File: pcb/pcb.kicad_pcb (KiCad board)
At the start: 2 copper layers, 65.5 x 70.5 mm, 22 parts, among them J1 Pump Back, J10 Temp & RH I2C, J2 Pump Front, J3 Electrovalve, J4 GPS, J5 Power, J6 APM, J7 Flowmeter, J8 OPC, J9 Pressure I2C, U1 LoRa, U2 MICRO SD

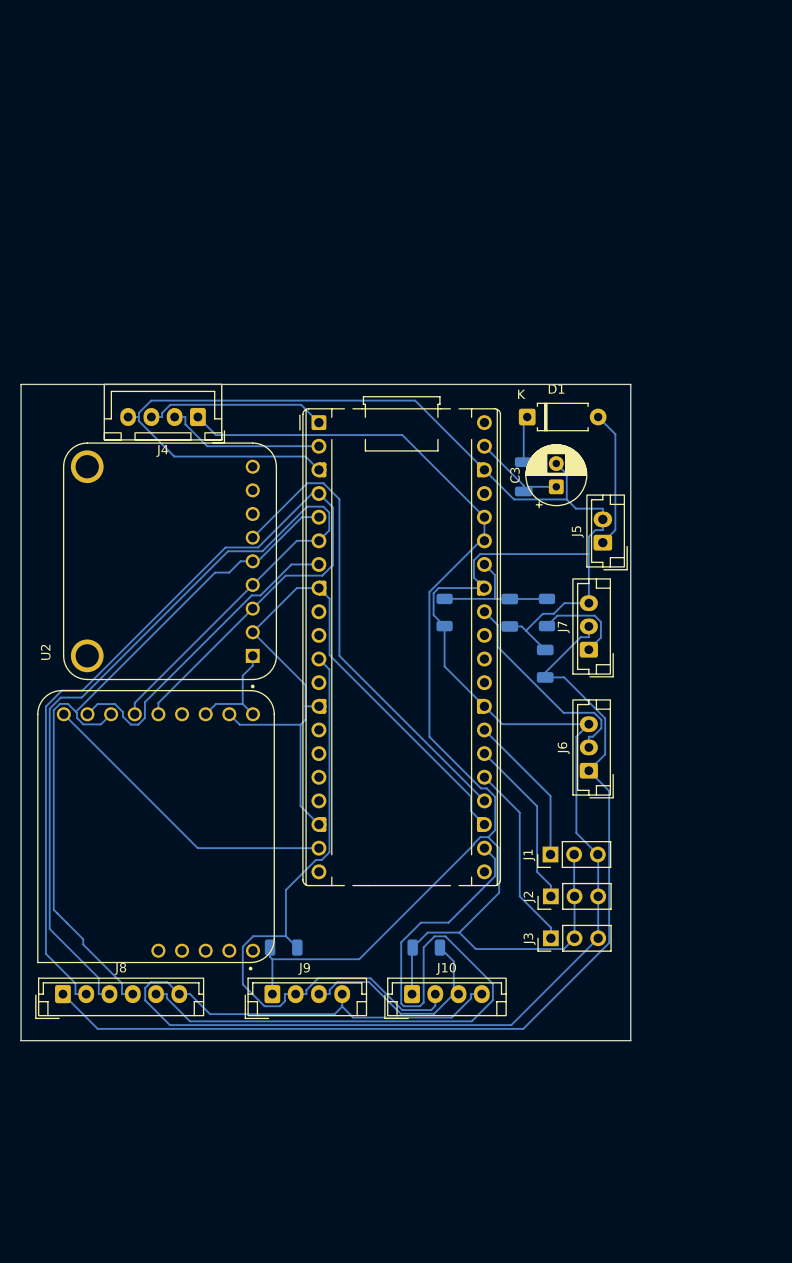
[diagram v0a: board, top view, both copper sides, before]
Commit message: New components layout
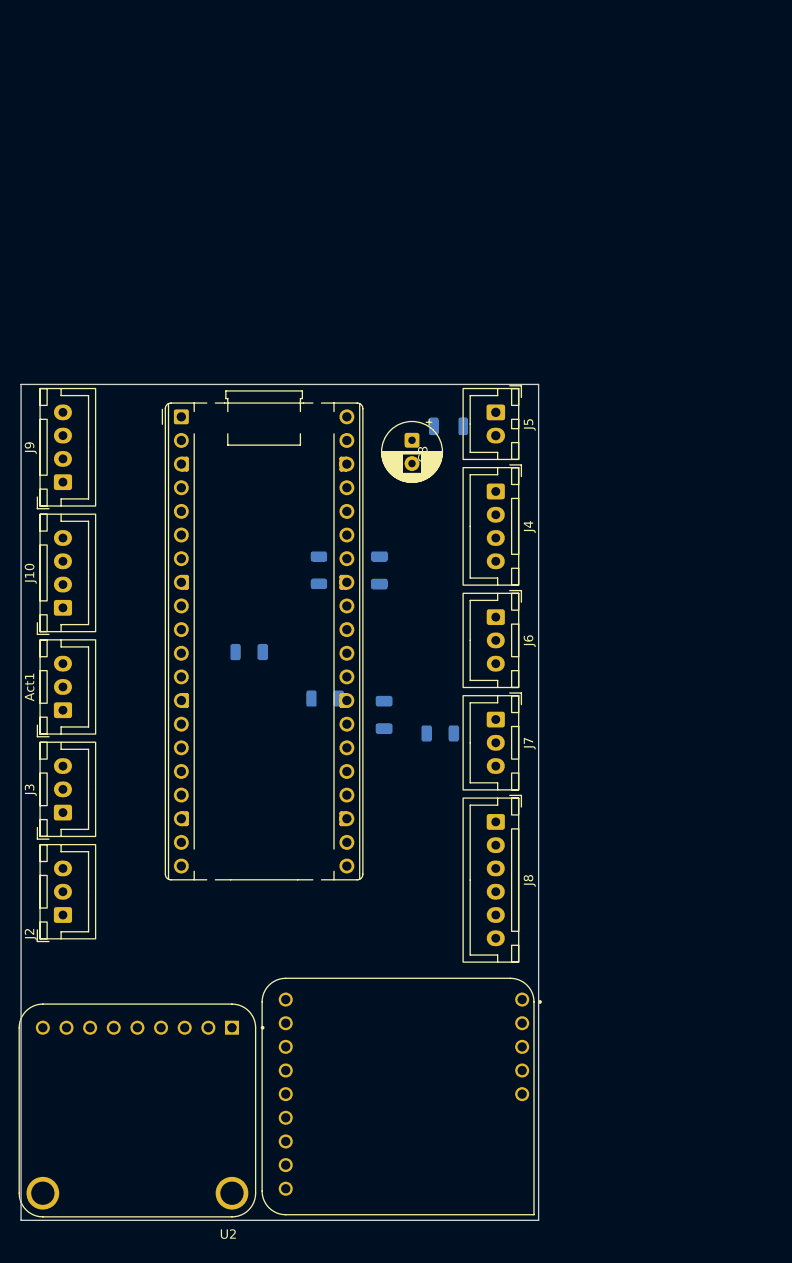
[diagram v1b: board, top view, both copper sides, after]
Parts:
- removed D1: D_Schottky, Diode_THT:D_A-405_P7.62mm_Horizontal
- Act1: renamed from J1; footprint Connector_PinHeader_2.54mm:PinHeader_1x03_P2.54mm_Vertical -> Connector_JST:JST_XH_B3B-XH-A_1x03_P2.50mm_Vertical
- J10, J9: footprint Connector_JST:JST_EH_B4B-EH-A_1x04_P2.50mm_Vertical -> Connector_JST:JST_XH_B4B-XH-A_1x04_P2.50mm_Vertical
- J2, J3: footprint Connector_PinHeader_2.54mm:PinHeader_1x03_P2.54mm_Vertical -> Connector_JST:JST_XH_B3B-XH-A_1x03_P2.50mm_Vertical
- J5: footprint Connector_JST:JST_EH_B2B-EH-A_1x02_P2.50mm_Vertical -> Connector_JST:JST_XH_B2B-XH-A_1x02_P2.50mm_Vertical
- J6, J7: footprint Connector_JST:JST_EH_B3B-EH-A_1x03_P2.50mm_Vertical -> Connector_JST:JST_XH_B3B-XH-A_1x03_P2.50mm_Vertical
- J8: footprint Connector_JST:JST_EH_B6B-EH-A_1x06_P2.50mm_Vertical -> Connector_JST:JST_XH_B6B-XH-A_1x06_P2.50mm_Vertical
- moved J9 59.4 mm to (105.0, 52.5), turned to 90 degrees
- moved U2 59.1 mm to (113.0, 120.0), turned to 180 degrees
- moved J10 55.9 mm to (105.0, 66.0), turned to 90 degrees
- moved Act1 54.6 mm to (105.0, 77.0)
- moved J3 54.1 mm to (105.0, 88.0)
- moved J2 52.5 mm to (105.0, 99.0)
- moved J8 50.0 mm to (151.5, 89.0), turned to -90 degrees
- moved U1 38.9 mm to (141.0, 118.5), turned to 0 degrees
- moved J4 33.0 mm to (151.5, 53.5), turned to -90 degrees
- moved R1 32.0 mm to (125.0, 70.8), turned to 180 degrees
- moved R2 28.9 mm to (133.2, 75.8), turned to 180 degrees
- moved J6 19.3 mm to (151.5, 67.0), turned to -90 degrees
- moved C2 18.2 mm to (139.5, 77.5)
- moved J5 18.1 mm to (151.5, 45.0), turned to -90 degrees
- moved R3 17.3 mm to (145.5, 79.5), turned to 180 degrees
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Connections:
- A1 pad 39: /3.3Vin -> /VSYS
- C3 pad 1: /3.3Vin -> /VSYS
- FB1 pad 1: Net-(D1-K) -> Net-(J5-Pin_1)
- FB1 pad 2: /3.3Vin -> /VSYS
- J5 pad 1: Net-(D1-A) -> Net-(J5-Pin_1)
- U1 pad JP3_1: /3.3V -> /VSYS
- U2 pad 1: /3.3V -> /VSYS
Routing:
- net GND: track 351.6 -> 0.00 mm
- net /3.3V: track 167.1 -> 0.00 mm
- net /SPI_SCK: track 106.6 -> 0.00 mm
- net /5V: track 106.0 -> 0.00 mm
- net /SPI_MISO: track 105.0 -> 0.00 mm
- net /OPC_CS: track 82.1 -> 0.00 mm
- net /SPI_MOSI: track 77.6 -> 0.00 mm
- net /I2C_SDA: track 69.9 -> 0.00 mm
- net /SD_CS: track 51.3 -> 0.00 mm
- net /LORA_CS: track 34.6 -> 0.00 mm
- net /LORA_RST: track 33.4 -> 0.00 mm
- net /I2C_SCL: track 23.7 -> 0.00 mm
- net /BAT_VOLT_ADC: track 22.5 -> 0.00 mm
- net /VALVE: track 20.3 -> 0.00 mm
- net /GPS_TX: track 19.6 -> 0.00 mm
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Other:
- board size 65.5 x 70.5 mm -> 55.6 x 89.8 mm

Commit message: new layout
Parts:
- moved Act1 49.9 mm to (151.5, 95.0), turned to -90 degrees
- moved J4 46.5 mm to (105.0, 52.5), turned to 90 degrees
- moved J9 27.0 mm to (105.0, 79.5)
- moved J7 24.0 mm to (151.5, 54.0)
- moved R2 19.7 mm to (113.5, 74.0), turned to 0 degrees
- moved R3 17.8 mm to (142.5, 62.0), turned to 90 degrees
- moved J3 13.5 mm to (105.0, 101.5)
- moved J8 12.5 mm to (151.5, 76.5)
- moved R1 11.6 mm to (113.5, 69.5), turned to 0 degrees
- moved J2 8.50 mm to (105.0, 90.5)
- moved U2 3.41 mm to (113.3, 116.6)
- moved C2 1.58 mm to (140.0, 76.0), turned to 180 degrees
- moved A1 1.52 mm to (118.5, 44.2)
- moved FB1 1.50 mm to (146.5, 45.0)
- moved J6 1.50 mm to (151.5, 65.5)
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
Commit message: v1 sent to JLCPCB
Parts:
- added SW1: SW_Push, Button_Switch_THT:SW_PUSH_6mm, F.Cu at (145.5, 71.5)
- moved R2 22.6 mm to (123.0, 53.5), turned to 180 degrees
- moved C2 18.6 mm to (146.5, 58.5), turned to -90 degrees
- moved J1 17.5 mm to (151.5, 77.5)
- moved R1 16.5 mm to (123.0, 56.0), turned to 180 degrees
- moved J8 12.5 mm to (151.5, 89.0)
- moved U2 2.89 mm to (113.5, 119.5)
- moved J3 2.50 mm to (105.0, 104.0)
- moved J2 2.00 mm to (105.0, 92.5)
- moved A1 1.76 mm to (118.5, 45.9)
- moved C3 1.50 mm to (142.5, 48.5)
- moved J9 1.50 mm to (105.0, 81.0)
- moved R3 1.08 mm to (143.0, 61.0), turned to 180 degrees
- moved J10 1.00 mm to (105.0, 67.0)
- moved C1 0.76 mm to (139.5, 62.5)
- moved FB1 0.50 mm to (146.5, 45.5)
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- renumbered Act1 to J1
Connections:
- A1 pad 10: unconnected-(A1-GPIO7-Pad10) -> /VALVE
- A1 pad 11: /I2C_SDA -> unconnected-(A1-GPIO8-Pad11)
- A1 pad 12: /I2C_SCL -> /SD_CS
- A1 pad 14: unconnected-(A1-GPIO10-Pad14) -> /SPI_SCK
- A1 pad 15: unconnected-(A1-GPIO11-Pad15) -> /SPI_MOSI
- A1 pad 16: unconnected-(A1-GPIO12-Pad16) -> /SPI_MISO
- A1 pad 19: /LORA_RST -> unconnected-(A1-GPIO14-Pad19)
- A1 pad 21: unconnected-(A1-GPIO16-Pad21) -> /LORA_CS
- A1 pad 24: /SD_CS -> unconnected-(A1-GPIO18-Pad24)
- A1 pad 25: /VALVE -> unconnected-(A1-GPIO19-Pad25)
- A1 pad 26: /PUMP_FRONT -> unconnected-(A1-GPIO20-Pad26)
- A1 pad 30: unconnected-(A1-RUN-Pad30) -> Net-(A1-RUN)
- A1 pad 4: /SPI_SCK -> /I2C_SDA
- A1 pad 5: /SPI_MOSI -> /I2C_SCL
- A1 pad 6: /SPI_MISO -> unconnected-(A1-GPIO4-Pad6)
- A1 pad 7: /LORA_CS -> unconnected-(A1-GPIO5-Pad7)
- A1 pad 9: unconnected-(A1-GPIO6-Pad9) -> /PUMP_FRONT
- J10 pad 2: /I2C_SDA -> /I2C_SCL
- J10 pad 3: /I2C_SCL -> /I2C_SDA
- J2 pad 1: /PUMP_FRONT -> GND
- J2 pad 3: GND -> /PUMP_FRONT
- J3 pad 1: /VALVE -> GND
- J3 pad 3: GND -> /VALVE
- J4 pad 2: /GPS_RX -> GND
- J4 pad 3: /GPS_TX -> /GPS_RX
- J4 pad 4: GND -> /GPS_TX
- J8 pad 2: /SPI_SCK -> GND
- J8 pad 3: /SPI_MISO -> /OPC_CS
- J8 pad 4: /SPI_MOSI -> /SPI_SCK
- J8 pad 5: /OPC_CS -> /SPI_MISO
- J8 pad 6: GND -> /SPI_MOSI
- J9 pad 2: /I2C_SDA -> /I2C_SCL
- J9 pad 3: /I2C_SCL -> /I2C_SDA
- R1 pad 2: /I2C_SDA -> /I2C_SCL
- R2 pad 2: /I2C_SCL -> /I2C_SDA
- U1 pad JP3_3: /3.3V -> unconnected-(U1-EN-PadJP3_3)
- U1 pad JP3_9: /LORA_RST -> unconnected-(U1-RST-PadJP3_9)
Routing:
- net /3.3V: track 0.00 -> 202.6 mm
- net /SPI_MOSI: track 0.00 -> 83.3 mm
- net /VSYS: track 0.00 -> 80.5 mm
- net /SPI_SCK: track 0.00 -> 78.5 mm
- net /SPI_MISO: track 0.00 -> 76.1 mm
- net /LORA_CS: track 0.00 -> 56.8 mm
- net GND: track 0.00 -> 42.6 mm
- net /5V: track 0.00 -> 42.3 mm
- net /SD_CS: track 0.00 -> 39.9 mm
- net /I2C_SDA: track 0.00 -> 37.0 mm
- net /VALVE: track 0.00 -> 35.8 mm
- net /I2C_SCL: track 0.00 -> 35.2 mm
- net /PUMP_FRONT: track 0.00 -> 26.8 mm
- net /PUMP_BACK: track 0.00 -> 21.5 mm
- net /OPC_CS: track 0.00 -> 16.2 mm
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- added copper zone on F.Cu, net GND
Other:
- board size 55.6 x 89.8 mm -> 56 x 90 mm
- board text added: "ACT1"
- board text added: "ACT2"
- board text added: "ACT3"
- board text added: "APM"
- board text added: "FLOW"
- board text added: "G.-"
- board text added: "GPS"
- board text added: "OPC"
- board text added: "PRES"
- board text added: "PWR"
- board text added: "T&RH"
